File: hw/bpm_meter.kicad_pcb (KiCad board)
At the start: 2 copper layers, 55 x 73.5 mm, 85 parts, among them J1 Conn_01x06_Pin, J2 Conn_01x03_Pin, J901 USB_C_Receptacle_USB2.0, Q1 AO3400A, SW901 SW_MEC_5E, U1 AOZ1282CI, U10 IS31FL3236A, U11 SLS0391FR1A1GD, U12 SLS0391FR1A1GD, U13 SLS0391FR1A1GD, U2 AMS1117-3.3, U3 H11L1, U901 RP2040, U902 AMS1117-3.3, U903 W25Q128JVS, Y901 Crystal_GND24_Small

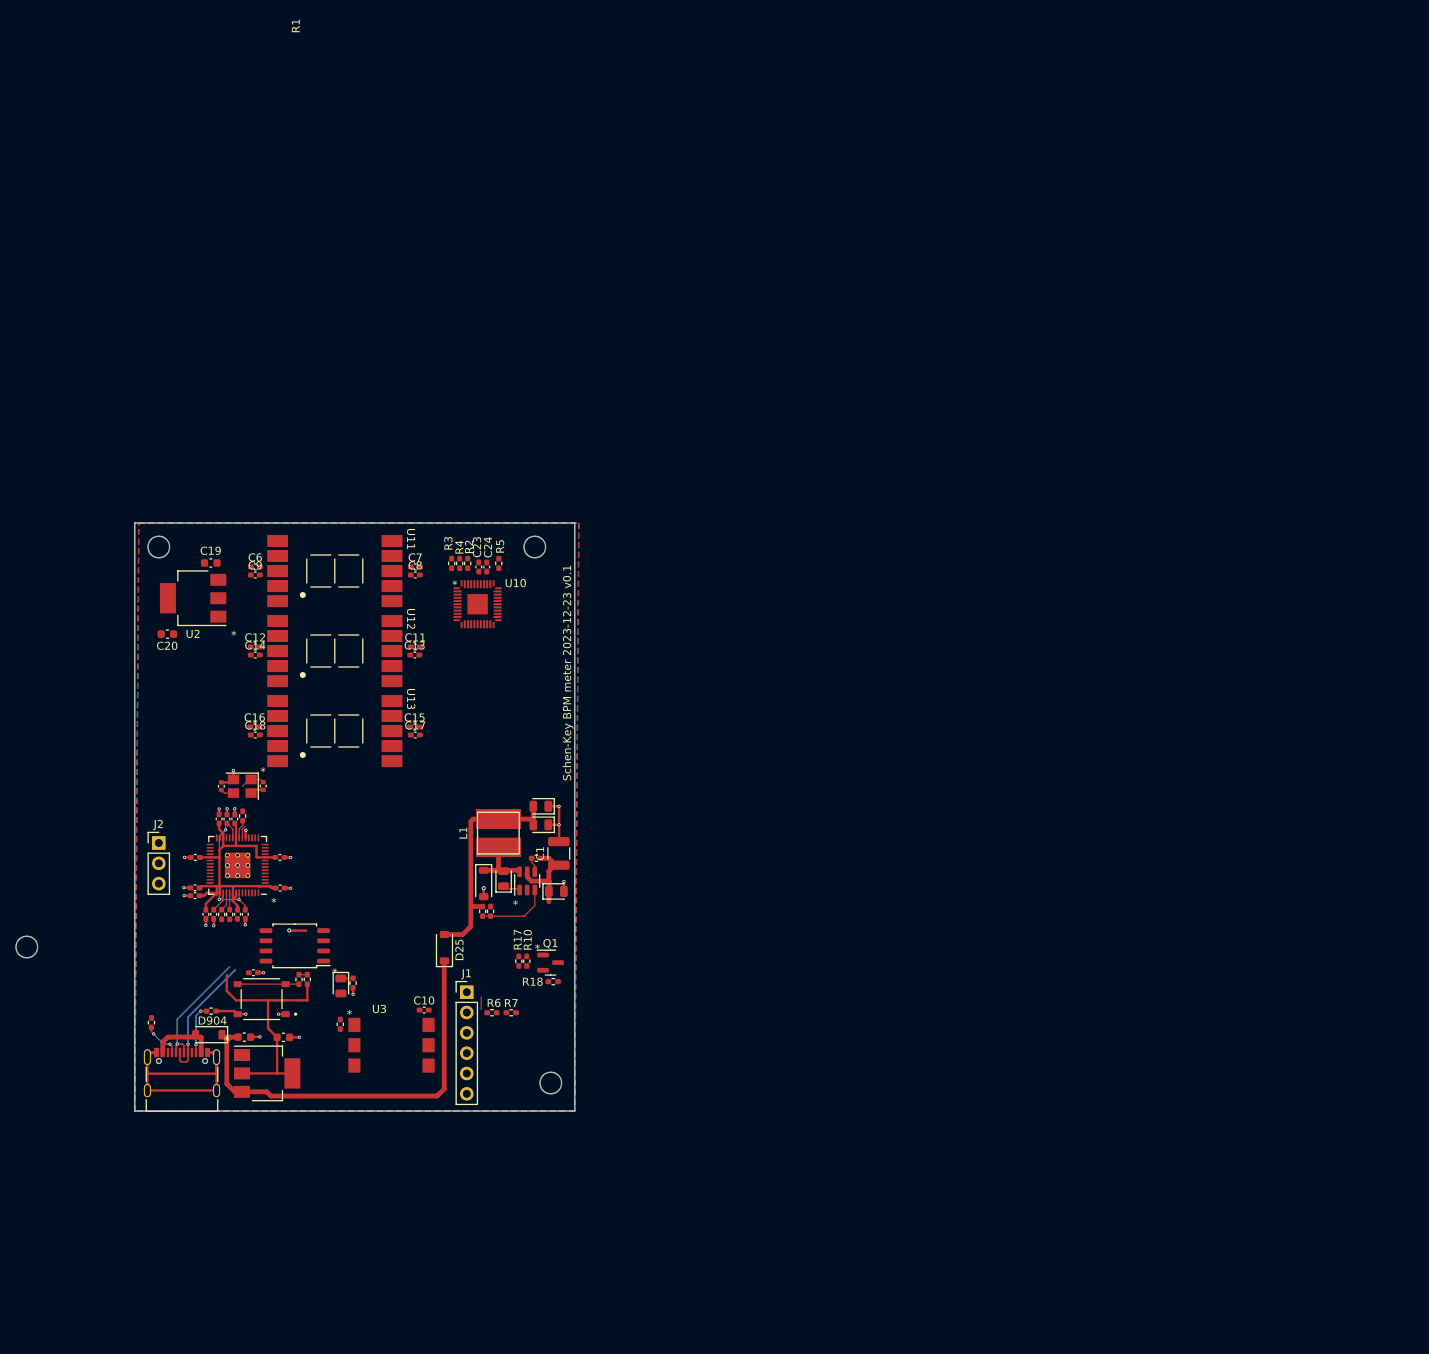
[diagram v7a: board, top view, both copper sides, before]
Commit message: Fixed the PCB outlines and placement of some components
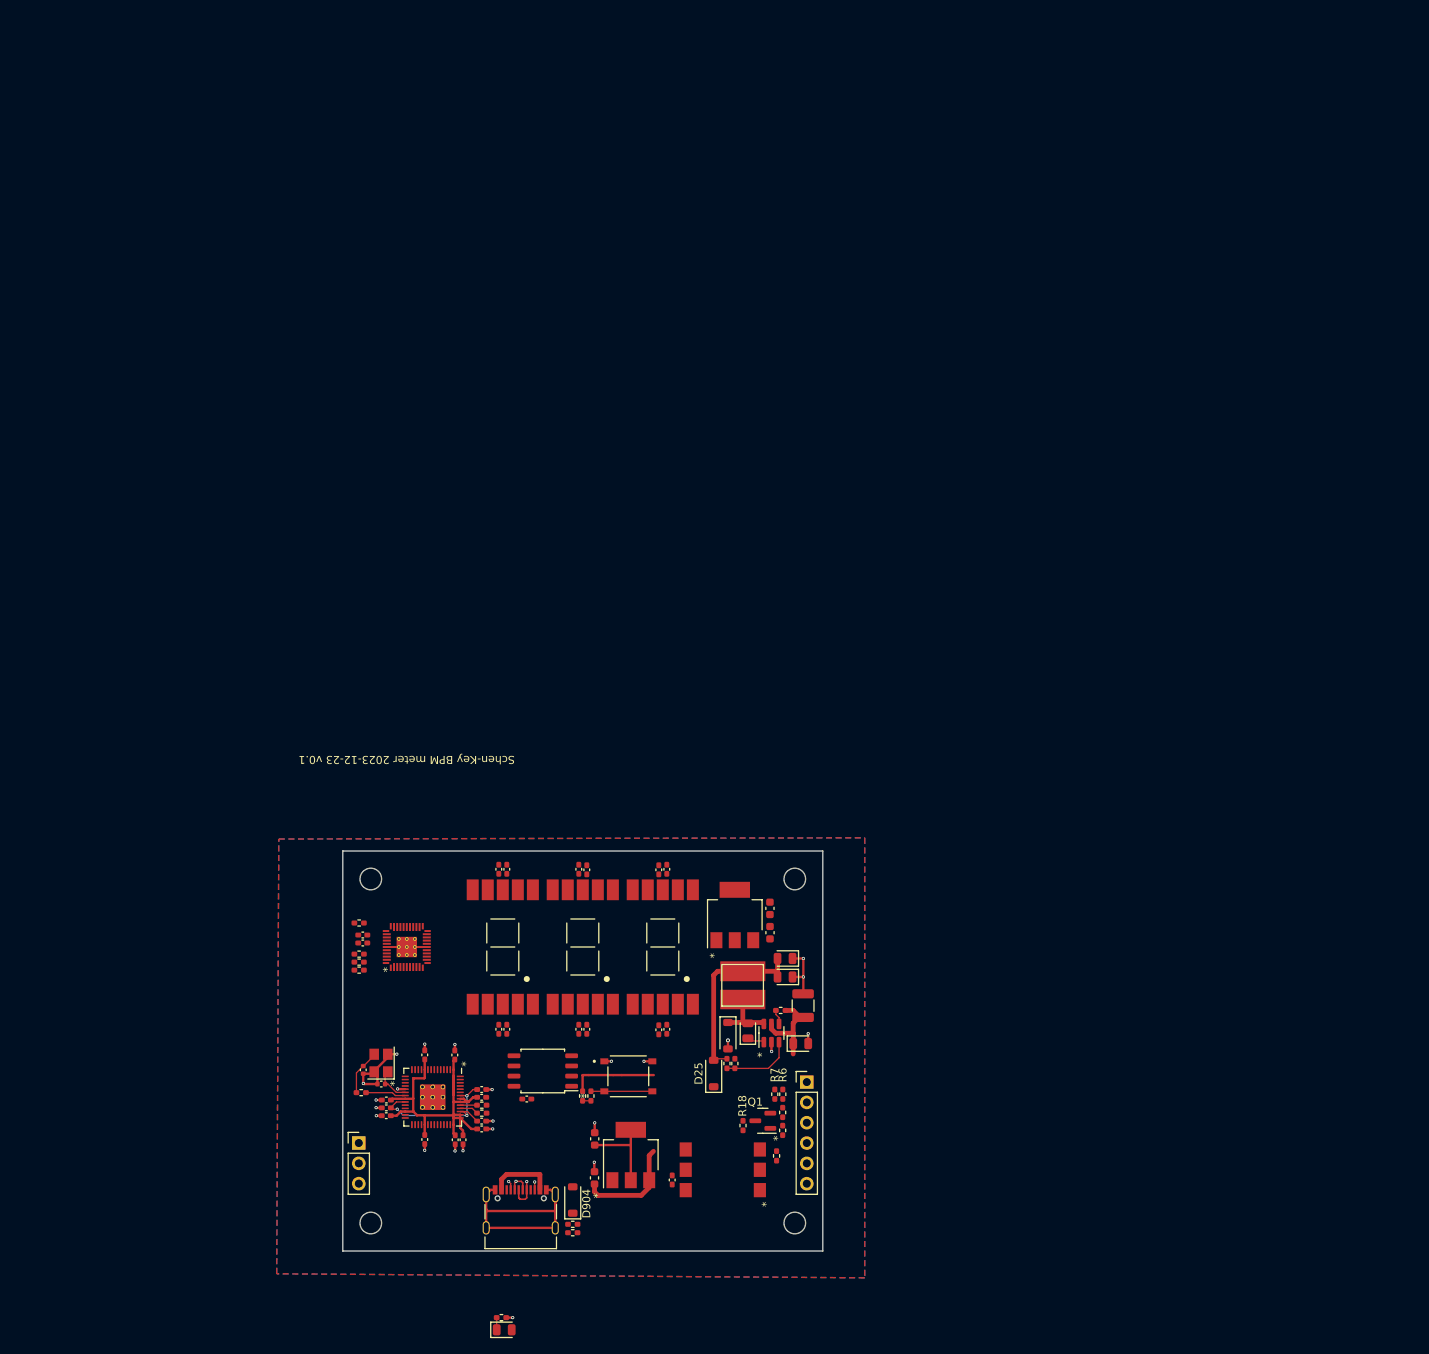
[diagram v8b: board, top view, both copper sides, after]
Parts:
- moved H4 102.0 mm to (156.5, 146.5), turned to 90 degrees
- moved H1 88.6 mm to (103.5, 146.5), turned to 90 degrees
- moved C19 83.8 mm to (153.4, 110.2), turned to 90 degrees
- moved C20 82.8 mm to (153.4, 107.2), turned to -90 degrees
- moved U2 78.4 mm to (149.0, 108.0), turned to -90 degrees
- moved C6 65.3 mm to (119.5, 122.3), turned to 90 degrees
- moved C9 64.9 mm to (120.5, 122.3), turned to 90 degrees
- moved C18 63.2 mm to (140.5, 122.3), turned to 90 degrees
- moved C16 63.1 mm to (139.5, 122.3), turned to 90 degrees
- moved C12 62.6 mm to (129.5, 122.3), turned to 90 degrees
- moved C14 62.5 mm to (130.5, 122.3), turned to 90 degrees
- moved R901 58.8 mm to (128.7, 147.7), turned to 0 degrees
- moved R1 57.0 mm to (154.2, 138.1), turned to 90 degrees
- moved R902 52.5 mm to (128.7, 146.7)
- moved R3 52.1 mm to (102.0, 114.9), turned to 0 degrees
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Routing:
- net +5V: track 52.3 -> 13.1 mm
- net /cpu/USB_D-: track 15.3 -> 2.93 mm
- net /cpu/USB_D+: track 16.0 -> 4.19 mm
- net +3V3: track 73.7 -> 66.7 mm
- net Net-(D25-A): track 29.2 -> 23.6 mm
- net Net-(J901-CC2): track 6.13 -> 0.99 mm, vias 2 -> 1
- net GND: track 65.1 -> 69.3 mm
- net Net-(C910-Pad1): track 1.68 -> 5.74 mm
- net Net-(J901-CC1): track 4.63 -> 1.14 mm, vias 2 -> 1
- net /cpu/XOUT: track 2.31 -> 5.05 mm
- net +14V: track 12.2 -> 10.6 mm
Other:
- board size 55 x 73.5 mm -> 60 x 50 mm
